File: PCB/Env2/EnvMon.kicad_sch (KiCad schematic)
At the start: 37 parts, among them J1 LCD, J2 DC, J3 TEMP, J4 LCD, J5 Reset, J6 USB-C-Socket-H, J7 TC2030-USB-NL-DS, J8 T6793, U1 ESP32-S3-MINI-1, U2 SCD41, U3 MD8942, U7 SHT40, U8 VEML6040

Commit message: Tracked and SS
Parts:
- removed C5: 100nF, RevK:C_0402, symbol Device:C
- removed U7: SHT40, RevK:Sensirion_DFN-4_1.5x1.5mm_P0.5mm_SHT4x, symbol RevK:SHT40
- added C6: 100nF, RevK:C_0402, symbol Device:C
- added R6, R7: 10K, RevK:R_0402, symbol Device:R
- added U4: MCP9808_MSOP, Package_SO:MSOP-8_3x3mm_P0.65mm, symbol Sensor_Temperature:MCP9808_MSOP
- J4: footprint RevK:PinSocket_1x08_P2.54mm_Vertical_SMD -> RevK:PinHeader_1x08_P2.54mm_Vertical; now not fitted; now left out of the parts list
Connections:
- net +3V3 is gone; now on net +3.3V: C4.1
- net +3.3V: now also C6.1, R6.1, R7.1, U4.8 (V_{DD}); no longer U1.18 (GPIO14)
- net BL: now also U1.13 (GPIO9)
- net CLK: now also U1.9 (GPIO5)
- net CS: now also U1.10 (GPIO6)
- net DC: now also U1.11 (GPIO7); no longer D19.1 (K), D20.1 (K), U3.5 (VIN)
- net DIN: now also U1.8 (GPIO4)
- net GND: now also C6.2, U4.4 (GND), U4.5 (A2), U4.6 (A1), U4.7 (A0)
- net LED: now also U1.32 (GPIO36); no longer U1.41 (GPIO45)
- net RST: now also U1.12 (GPIO8)
- net SCL: now also R6.2, U4.2 (SCL)
- net SDA: now also R7.2, U4.1 (SDA)
- new net VDC: D19.1 (K), D20.1 (K), U3.5 (VIN)
- no-connect marks 25 -> 29

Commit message: Tweaks and render
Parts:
- added J10, J11, J12, J9: Conn_01x01, RevK:PinHeader_1x01_P2.54mm_Vertical, symbol Connector_Generic:Conn_01x01
- J8: footprint Connector_PinSocket_2.54mm:PinSocket_1x06_P2.54mm_Vertical -> RevK:PinHeader_1x06_P2.54mm_Vertical
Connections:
- no-connect marks 29 -> 33

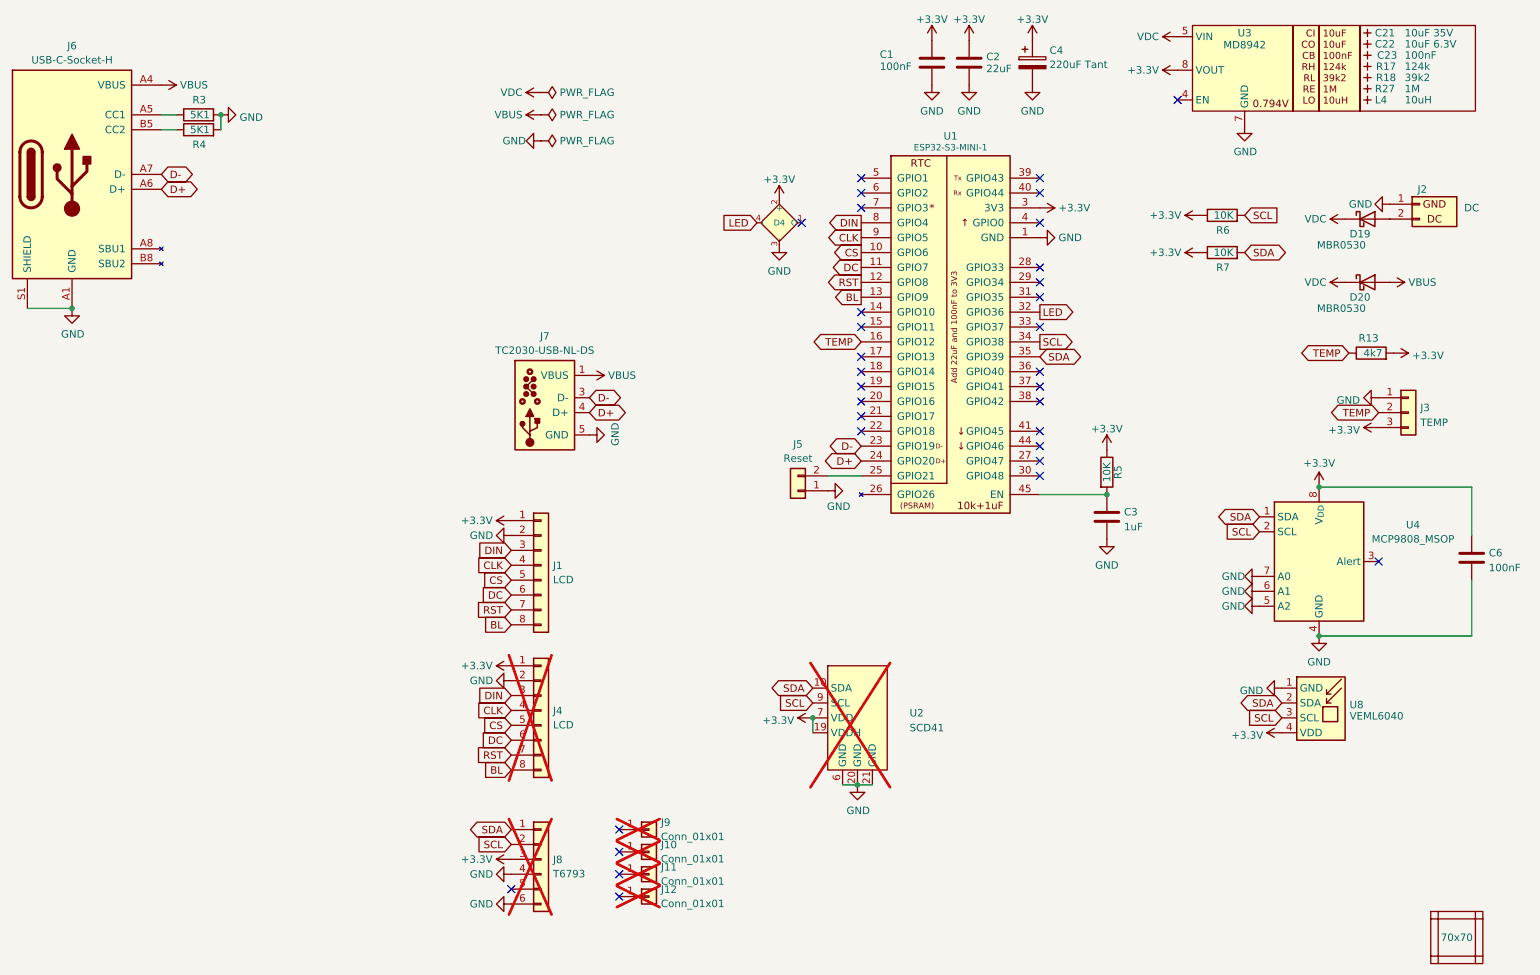
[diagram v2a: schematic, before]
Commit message: Pressure sensor
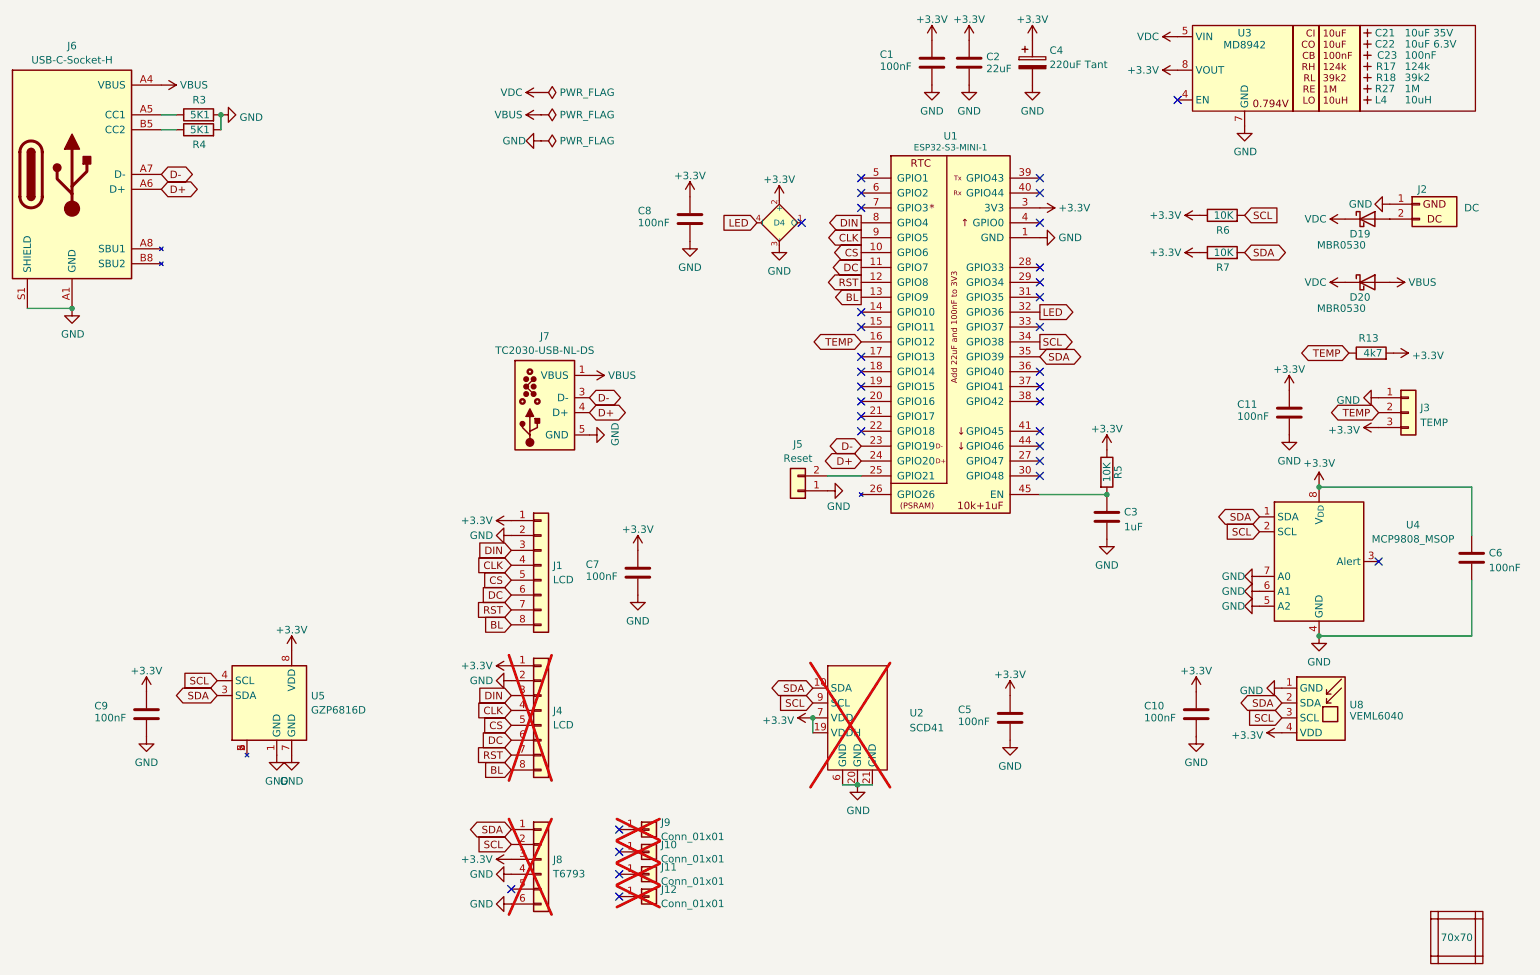
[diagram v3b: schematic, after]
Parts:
- added C10, C11, C5, C7, C8, C9: 100nF, RevK:C_0402, symbol Device:C
- added U5: GZP6816D, Package_LGA:Bosch_LGA-8_2x2.5mm_P0.65mm_ClockwisePinNumbering, symbol RevK:GZP6816D
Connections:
- net +3.3V: now also C10.1, C11.1, C5.1, C7.1, C8.1, C9.1, U5.8 (VDD)
- net GND: now also C10.2, C11.2, C5.2, C7.2, C8.2, C9.2, U5.1 (GND), U5.7 (GND)
- net SCL: now also U5.4 (SCL)
- net SDA: now also U5.3 (SDA)
- new net: U5.2, U5.5, U5.6
